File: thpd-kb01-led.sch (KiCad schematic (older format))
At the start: 102 parts

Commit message: WIP
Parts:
- removed D113, D114, D115, D116, D117, D118, D119, D120, D121, D122, D123, D124, D125, D126, D127, D128, D129, D130, D131, D132, D133, D134, D135, D136, D137, D138, D139, D140, D141, D142, D143, D144, D145, D146, D147, D148, D149, D150, D151, D152, D153, D154, D155, D156, D157, D158, D159, D160, D161, D162, D163, D164, D165, D166, D167, D168, D169, D170, D171, D172, D173, D174, D175, D176, D177, D178, D179, D180, D181, D182, D183, D184, D185, D186, D187, D188, D189, D190, D191, D192, D193, D194, D195, D196, D197, D198, D199, D200, D201, D202, D203: SK6812, thpd-kb01-custom:LED_SK6812MINI-ER_PLCC4_3.5x2.8mm_P1.8mm, symbol LED:SK6812
- added LED100, LED101, LED11, LED12, LED13, LED14, LED15, LED16, LED17, LED18, LED19, LED20, LED21, LED22, LED23, LED24, LED25, LED26, LED27, LED28, LED29, LED30, LED31, LED32, LED33, LED34, LED35, LED36, LED37, LED38, LED39, LED40, LED41, LED42, LED43, LED44, LED45, LED46, LED47, LED48, LED49, LED50, LED51, LED52, LED53, LED54, LED55, LED56, LED57, LED58, LED59, LED60, LED61, LED62, LED63, LED64, LED65, LED66, LED67, LED68, LED69, LED70, LED71, LED72, LED73, LED74, LED75, LED76, LED77, LED78, LED79, LED80, LED81, LED82, LED83, LED84, LED85, LED86, LED87, LED88, LED89, LED90, LED91, LED92, LED93, LED94, LED95, LED96, LED97, LED98, LED99: SK6812, thpd-kb01-custom:LED_SK6812MINI-ER_PLCC4_3.5x2.8mm_P1.8mm, symbol LED:SK6812
- renumbered D103 to LED1, D112 to LED10, D104 to LED2, D105 to LED3, D106 to LED4, D107 to LED5, D108 to LED6, D109 to LED7, D110 to LED8, D111 to LED9
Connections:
- net +3V3: now also LED100.3 (VDD), LED101.3 (VDD), LED11.3 (VDD), LED12.3 (VDD), LED13.3 (VDD), LED14.3 (VDD), LED15.3 (VDD), LED16.3 (VDD), LED17.3 (VDD), LED18.3 (VDD), LED19.3 (VDD), LED20.3 (VDD), LED21.3 (VDD), LED22.3 (VDD), LED23.3 (VDD), LED24.3 (VDD), LED25.3 (VDD), LED26.3 (VDD), LED27.3 (VDD), LED28.3 (VDD), LED29.3 (VDD), LED30.3 (VDD), LED31.3 (VDD), LED32.3 (VDD), LED33.3 (VDD), LED34.3 (VDD), LED35.3 (VDD), LED36.3 (VDD), LED37.3 (VDD), LED38.3 (VDD), LED39.3 (VDD), LED40.3 (VDD), LED41.3 (VDD), LED42.3 (VDD), LED43.3 (VDD), LED44.3 (VDD), LED45.3 (VDD), LED46.3 (VDD), LED47.3 (VDD), LED48.3 (VDD), LED49.3 (VDD), LED50.3 (VDD), LED51.3 (VDD), LED52.3 (VDD), LED53.3 (VDD), LED54.3 (VDD), LED55.3 (VDD), LED56.3 (VDD), LED57.3 (VDD), LED58.3 (VDD), LED59.3 (VDD), LED60.3 (VDD), LED61.3 (VDD), LED62.3 (VDD), LED63.3 (VDD), LED64.3 (VDD), LED65.3 (VDD), LED66.3 (VDD), LED67.3 (VDD), LED68.3 (VDD), LED69.3 (VDD), LED70.3 (VDD), LED71.3 (VDD), LED72.3 (VDD), LED73.3 (VDD), LED74.3 (VDD), LED75.3 (VDD), LED76.3 (VDD), LED77.3 (VDD), LED78.3 (VDD), LED79.3 (VDD), LED80.3 (VDD), LED81.3 (VDD), LED82.3 (VDD), LED83.3 (VDD), LED84.3 (VDD), LED85.3 (VDD), LED86.3 (VDD), LED87.3 (VDD), LED88.3 (VDD), LED89.3 (VDD), LED90.3 (VDD), LED91.3 (VDD), LED92.3 (VDD), LED93.3 (VDD), LED94.3 (VDD), LED95.3 (VDD), LED96.3 (VDD), LED97.3 (VDD), LED98.3 (VDD), LED99.3 (VDD)
- net GND: now also LED100.1 (VSS), LED101.1 (VSS), LED11.1 (VSS), LED12.1 (VSS), LED13.1 (VSS), LED14.1 (VSS), LED15.1 (VSS), LED16.1 (VSS), LED17.1 (VSS), LED18.1 (VSS), LED19.1 (VSS), LED20.1 (VSS), LED21.1 (VSS), LED22.1 (VSS), LED23.1 (VSS), LED24.1 (VSS), LED25.1 (VSS), LED26.1 (VSS), LED27.1 (VSS), LED28.1 (VSS), LED29.1 (VSS), LED30.1 (VSS), LED31.1 (VSS), LED32.1 (VSS), LED33.1 (VSS), LED34.1 (VSS), LED35.1 (VSS), LED36.1 (VSS), LED37.1 (VSS), LED38.1 (VSS), LED39.1 (VSS), LED40.1 (VSS), LED41.1 (VSS), LED42.1 (VSS), LED43.1 (VSS), LED44.1 (VSS), LED45.1 (VSS), LED46.1 (VSS), LED47.1 (VSS), LED48.1 (VSS), LED49.1 (VSS), LED50.1 (VSS), LED51.1 (VSS), LED52.1 (VSS), LED53.1 (VSS), LED54.1 (VSS), LED55.1 (VSS), LED56.1 (VSS), LED57.1 (VSS), LED58.1 (VSS), LED59.1 (VSS), LED60.1 (VSS), LED61.1 (VSS), LED62.1 (VSS), LED63.1 (VSS), LED64.1 (VSS), LED65.1 (VSS), LED66.1 (VSS), LED67.1 (VSS), LED68.1 (VSS), LED69.1 (VSS), LED70.1 (VSS), LED71.1 (VSS), LED72.1 (VSS), LED73.1 (VSS), LED74.1 (VSS), LED75.1 (VSS), LED76.1 (VSS), LED77.1 (VSS), LED78.1 (VSS), LED79.1 (VSS), LED80.1 (VSS), LED81.1 (VSS), LED82.1 (VSS), LED83.1 (VSS), LED84.1 (VSS), LED85.1 (VSS), LED86.1 (VSS), LED87.1 (VSS), LED88.1 (VSS), LED89.1 (VSS), LED90.1 (VSS), LED91.1 (VSS), LED92.1 (VSS), LED93.1 (VSS), LED94.1 (VSS), LED95.1 (VSS), LED96.1 (VSS), LED97.1 (VSS), LED98.1 (VSS), LED99.1 (VSS)
- net at LED10.4 (DOUT): now also LED11.2 (DIN)
- new net: LED11.4 (DOUT), LED12.2 (DIN)
- new net: LED12.4 (DOUT), LED13.2 (DIN)
- new net: LED13.4 (DOUT), LED14.2 (DIN)
- new net: LED14.4 (DOUT), LED15.2 (DIN)
- new net: LED15.4 (DOUT), LED16.2 (DIN)
- new net: LED16.4 (DOUT), LED17.2 (DIN)
- new net: LED17.4 (DOUT), LED18.2 (DIN)
- new net: LED18.4 (DOUT), LED19.2 (DIN)
- new net: LED19.4 (DOUT), LED20.2 (DIN)
- new net: LED20.4 (DOUT), LED21.2 (DIN)
- new net: LED21.4 (DOUT), LED22.2 (DIN)
- new net: LED22.4 (DOUT), LED23.2 (DIN)
- new net: LED23.4 (DOUT), LED24.2 (DIN)
- new net: LED24.4 (DOUT), LED25.2 (DIN)
- new net: LED25.4 (DOUT), LED26.2 (DIN)
- new net: LED26.4 (DOUT), LED27.2 (DIN)
- new net: LED27.4 (DOUT), LED28.2 (DIN)
- new net: LED28.4 (DOUT), LED29.2 (DIN)
- new net: LED29.4 (DOUT), LED30.2 (DIN)
- new net: LED30.4 (DOUT), LED31.2 (DIN)
- new net: LED31.4 (DOUT), LED32.2 (DIN)
- new net: LED32.4 (DOUT), LED33.2 (DIN)
- new net: LED33.4 (DOUT), LED34.2 (DIN)
- new net: LED34.4 (DOUT), LED35.2 (DIN)
- new net: LED35.4 (DOUT), LED36.2 (DIN)
- new net: LED36.4 (DOUT), LED37.2 (DIN)
- new net: LED37.4 (DOUT), LED38.2 (DIN)
- new net: LED38.4 (DOUT), LED39.2 (DIN)
- new net: LED39.4 (DOUT), LED40.2 (DIN)
- new net: LED40.4 (DOUT), LED41.2 (DIN)
- new net: LED41.4 (DOUT), LED42.2 (DIN)
- new net: LED42.4 (DOUT), LED43.2 (DIN)
- new net: LED43.4 (DOUT), LED44.2 (DIN)
- new net: LED44.4 (DOUT), LED45.2 (DIN)
- new net: LED45.4 (DOUT), LED46.2 (DIN)
- new net: LED46.4 (DOUT), LED47.2 (DIN)
- new net: LED47.4 (DOUT), LED48.2 (DIN)
- new net: LED48.4 (DOUT), LED49.2 (DIN)
- new net: LED49.4 (DOUT), LED50.2 (DIN)
- new net: LED50.4 (DOUT), LED51.2 (DIN)
- new net: LED51.4 (DOUT), LED52.2 (DIN)
- new net: LED52.4 (DOUT), LED53.2 (DIN)
- new net: LED53.4 (DOUT), LED54.2 (DIN)
- new net: LED54.4 (DOUT), LED55.2 (DIN)
- new net: LED55.4 (DOUT), LED56.2 (DIN)
- new net: LED56.4 (DOUT), LED57.2 (DIN)
- new net: LED57.4 (DOUT), LED58.2 (DIN)
- new net: LED58.4 (DOUT), LED59.2 (DIN)
- new net: LED59.4 (DOUT), LED60.2 (DIN)
- new net: LED60.4 (DOUT), LED61.2 (DIN)
- new net: LED61.4 (DOUT), LED62.2 (DIN)
- new net: LED62.4 (DOUT), LED63.2 (DIN)
- new net: LED63.4 (DOUT), LED64.2 (DIN)
- new net: LED64.4 (DOUT), LED65.2 (DIN)
- new net: LED65.4 (DOUT), LED66.2 (DIN)
- new net: LED66.4 (DOUT), LED67.2 (DIN)
- new net: LED67.4 (DOUT), LED68.2 (DIN)
- new net: LED68.4 (DOUT), LED69.2 (DIN)
- new net: LED69.4 (DOUT), LED70.2 (DIN)
- new net: LED70.4 (DOUT), LED71.2 (DIN)
- new net: LED71.4 (DOUT), LED72.2 (DIN)
- new net: LED72.4 (DOUT), LED73.2 (DIN)
- new net: LED73.4 (DOUT), LED74.2 (DIN)
- new net: LED74.4 (DOUT), LED75.2 (DIN)
- new net: LED75.4 (DOUT), LED76.2 (DIN)
- new net: LED76.4 (DOUT), LED77.2 (DIN)
- new net: LED77.4 (DOUT), LED78.2 (DIN)
- new net: LED78.4 (DOUT), LED79.2 (DIN)
- new net: LED79.4 (DOUT), LED80.2 (DIN)
- new net: LED80.4 (DOUT), LED81.2 (DIN)
- new net: LED81.4 (DOUT), LED82.2 (DIN)
- new net: LED82.4 (DOUT), LED83.2 (DIN)
- new net: LED83.4 (DOUT), LED84.2 (DIN)
- new net: LED84.4 (DOUT), LED85.2 (DIN)
- new net: LED85.4 (DOUT), LED86.2 (DIN)
- new net: LED86.4 (DOUT), LED87.2 (DIN)
- new net: LED87.4 (DOUT), LED88.2 (DIN)
- new net: LED88.4 (DOUT), LED89.2 (DIN)
- new net: LED89.4 (DOUT), LED90.2 (DIN)
- new net: LED90.4 (DOUT), LED91.2 (DIN)
- new net: LED91.4 (DOUT), LED92.2 (DIN)
- new net: LED92.4 (DOUT), LED93.2 (DIN)
- new net: LED93.4 (DOUT), LED94.2 (DIN)
- new net: LED94.4 (DOUT), LED95.2 (DIN)
- new net: LED95.4 (DOUT), LED96.2 (DIN)
- new net: LED96.4 (DOUT), LED97.2 (DIN)
- new net: LED97.4 (DOUT), LED98.2 (DIN)
- new net: LED98.4 (DOUT), LED99.2 (DIN)
- new net: LED100.2 (DIN), LED99.4 (DOUT)
- new net: LED100.4 (DOUT), LED101.2 (DIN)

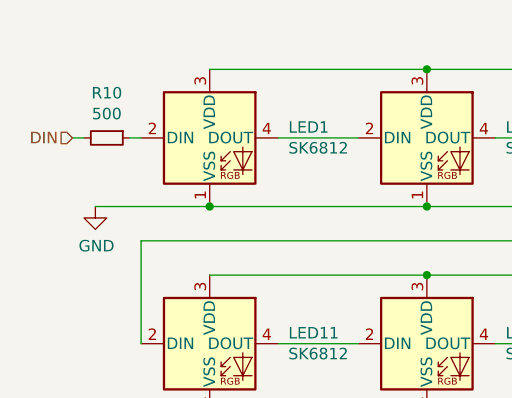
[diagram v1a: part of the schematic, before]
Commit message: Add LCSC part numbers and prepared for output.
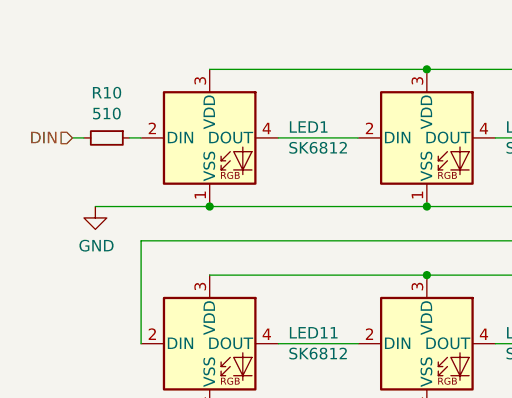
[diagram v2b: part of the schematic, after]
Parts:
- R10: value 500 -> 510; LCSC Part # (none) -> C25123
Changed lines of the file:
@@
 P 1450 1250
 F 0 "R10" V 1254 1250 50  0000 C CNN
-F 1 "500" V 1345 1250 50  0000 C CNN
+F 1 "510" V 1345 1250 50  0000 C CNN
 F 2 "Resistor_SMD:R_0402_1005Metric" H 1450 1250 50  0001 C CNN
 F 3 "~" H 1450 1250 50  0001 C CNN
+F 4 "C25123" H 1450 1250 50  0001 C CNN "LCSC Part #"
 	1    1450 1250
 	0    1    1    0
